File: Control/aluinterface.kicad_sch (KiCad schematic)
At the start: 11 parts, among them J10 Conn_01x02, J11 Conn_01x03, J9 Conn_01x01, U16 4078, U17 4078, U18 74AHC1G32, U19 74HC173

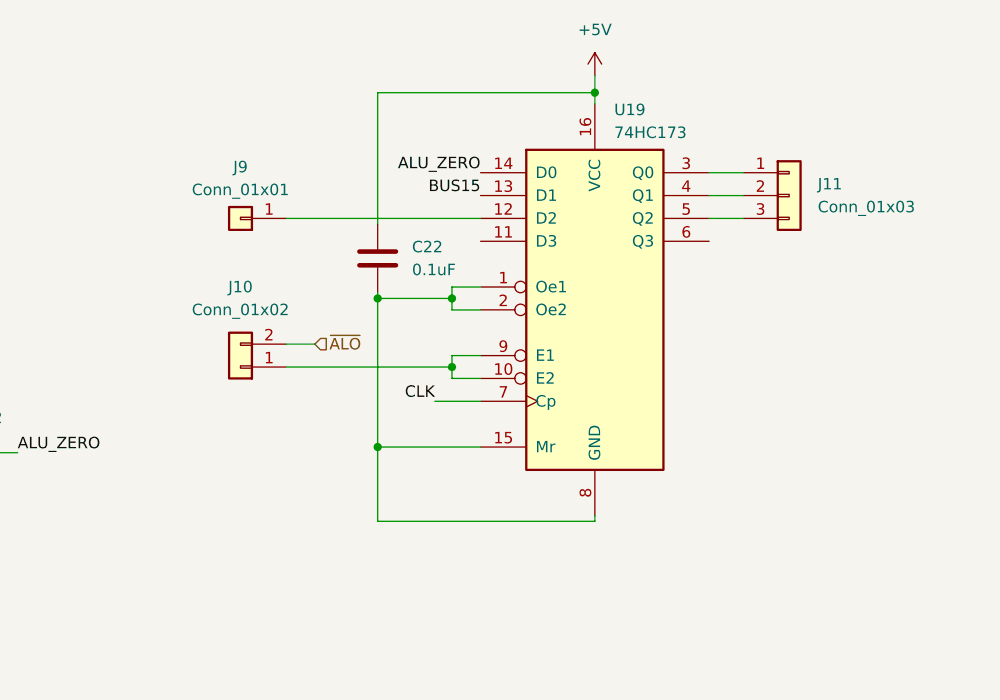
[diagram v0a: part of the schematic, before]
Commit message: Cleanup, added photos and README overhaul
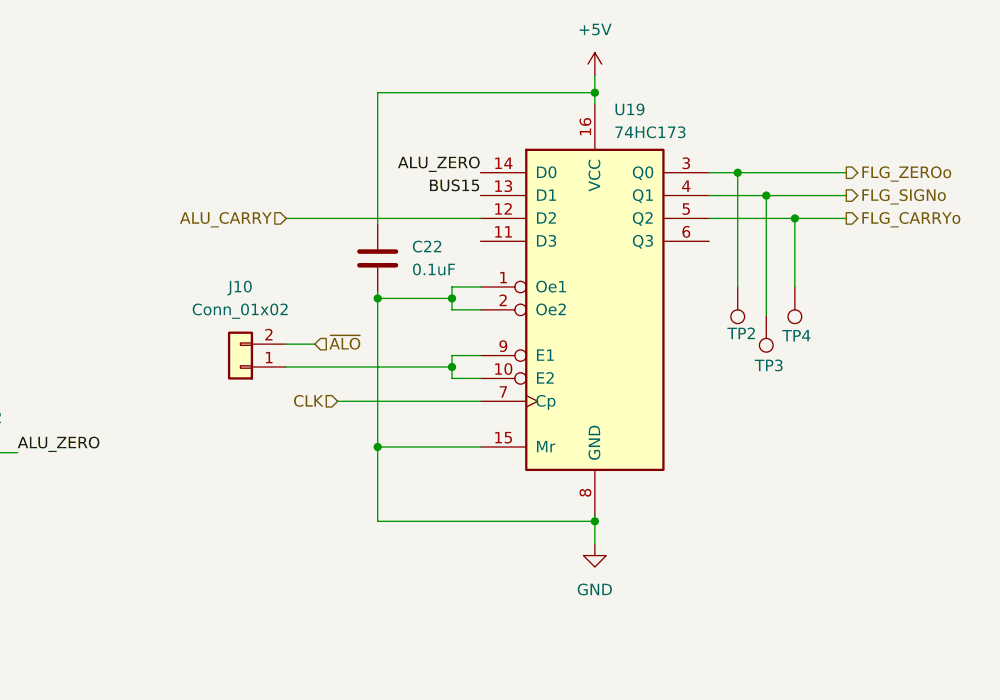
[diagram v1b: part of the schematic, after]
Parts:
- removed J11: Conn_01x03, Connector_PinHeader_2.54mm:PinHeader_1x03_P2.54mm_Vertical, symbol Connector_Generic:Conn_01x03
- removed J9: Conn_01x01, Connector_PinHeader_2.54mm:PinHeader_1x01_P2.54mm_Vertical, symbol Connector_Generic:Conn_01x01
- added TP2, TP3, TP4: TestPoint, TestPoint:TestPoint_Pad_D1.0mm, symbol Connector:TestPoint
- U16, U17: footprint Package_SO:SOIC-16_3.9x9.9mm_P1.27mm -> Package_SO:SOIC-14_3.9x8.7mm_P1.27mm
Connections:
- net GND: now also C22.2, U19.1 (Oe1), U19.15 (Mr), U19.2 (Oe2), U19.8 (GND)
- net ALU_CARRY: now reaches U19.12 (D2)
- net FLG_ZEROo: now reaches U19.3 (Q0)
- net FLG_ZEROo: now also TP2.1
- net FLG_SIGNo: now reaches U19.4 (Q1)
- net FLG_SIGNo: now also TP3.1
- net FLG_CARRYo: now reaches U19.5 (Q2)
- net FLG_CARRYo: now also TP4.1

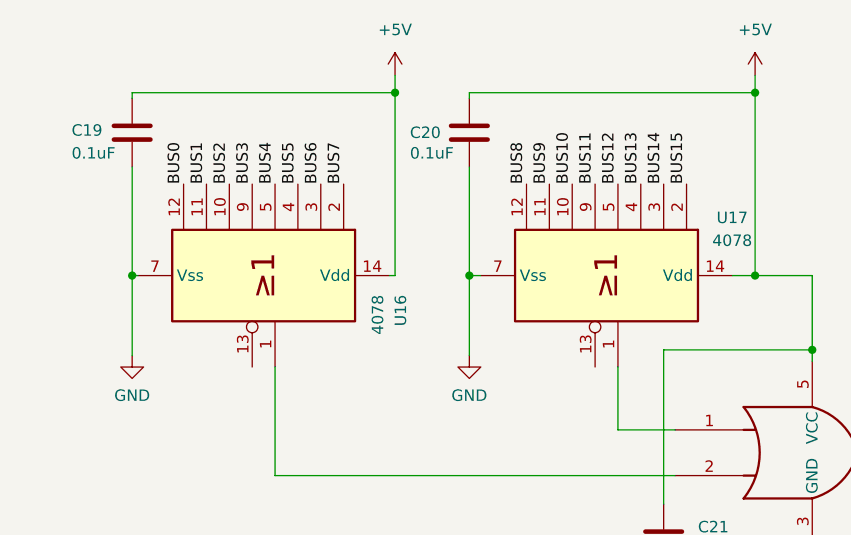
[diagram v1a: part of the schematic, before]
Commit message: Finalized Control unit for fabrication
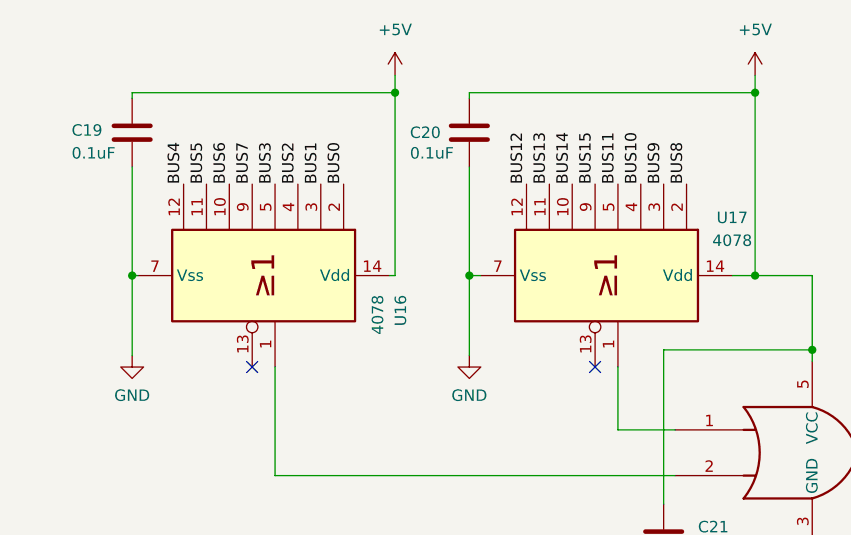
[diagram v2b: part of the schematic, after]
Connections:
- net BUS0: now also U16.2; no longer U16.12
- net BUS1: now also U16.3; no longer U16.11
- net BUS10: now also U17.4; no longer U17.10
- net BUS11: now also U17.5; no longer U17.9
- net BUS12: now also U17.12; no longer U17.5
- net BUS13: now also U17.11; no longer U17.4
- net BUS14: now also U17.10; no longer U17.3
- net BUS15: now also U17.9; no longer U17.2
- net BUS2: now also U16.4; no longer U16.10
- net BUS3: now also U16.5; no longer U16.9
- net BUS4: now also U16.12; no longer U16.5
- net BUS5: now also U16.11; no longer U16.4
- net BUS6: now also U16.10; no longer U16.3
- net BUS7: now also U16.9; no longer U16.2
- net BUS8: now also U17.2; no longer U17.12
- net BUS9: now also U17.3; no longer U17.11
- no-connect marks 0 -> 2
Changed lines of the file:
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@@
 		(color 0 0 0 0)
 	)
+	(no_connect
+		(at 106.68 55.245)
+	)
+	(no_connect
+		(at 68.58 55.245)
+	)
 	(bus_entry
 		(at 29.845 48.895)
@@
 		)
 	)
-	(label "BUS0"
+	(label "BUS4"
 		(at 60.96 34.925 90)
 		(effects
@@
 		)
 	)
-	(label "BUS13"
+	(label "BUS10"
 		(at 111.76 34.925 90)
 		(effects
@@
 		)
 	)
-	(label "BUS4"
+	(label "BUS3"
 		(at 71.12 34.925 90)
 		(effects
@@
 		)
 	)
-	(label "BUS15"
+	(label "BUS8"
 		(at 116.84 34.925 90)
 		(effects
@@
 		)
 	)
-	(label "BUS8"
+	(label "BUS12"
 		(at 99.06 34.925 90)
 		(effects
@@
 		)
 	)
-	(label "BUS3"
+	(label "BUS7"
 		(at 68.58 34.925 90)
 		(effects
@@
 		)
 	)
-	(label "BUS14"
+	(label "BUS9"
 		(at 114.3 34.925 90)
 		(effects
@@
 		)
 	)
-	(label "BUS9"
+	(label "BUS13"
 		(at 101.6 34.925 90)
 		(effects
@@
 		)
 	)
-	(label "BUS12"
+	(label "BUS11"
 		(at 109.22 34.925 90)
 		(effects
@@
 		)
 	)
-	(label "BUS10"
+	(label "BUS14"
 		(at 104.14 34.925 90)
 		(effects
@@
 		)
 	)
-	(label "BUS6"
+	(label "BUS1"
 		(at 76.2 34.925 90)
 		(effects
@@
 		)
 	)
-	(label "BUS1"
+	(label "BUS5"
 		(at 63.5 34.925 90)
 		(effects
@@
 		)
 	)
-	(label "BUS7"
+	(label "BUS0"
 		(at 78.74 34.925 90)
 		(effects
@@
 		)
 	)
-	(label "BUS11"
+	(label "BUS15"
 		(at 106.68 34.925 90)
 		(effects
@@
 		)
 	)
-	(label "BUS5"
+	(label "BUS2"
 		(at 73.66 34.925 90)
 		(effects
@@
 		)
 	)
-	(label "BUS2"
+	(label "BUS6"
 		(at 66.04 34.925 90)
 		(effects

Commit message: Updated control unit and finalized for fabrication
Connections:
- no-connect marks 2 -> 4
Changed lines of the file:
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@@
+	)
+	(no_connect
+		(at 201.93 41.275)
 	)
 	(no_connect
 		(at 68.58 55.245)
 	)
+	(no_connect
+		(at 227.33 41.275)
+	)
 	(bus_entry
